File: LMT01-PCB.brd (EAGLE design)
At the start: 87 x 34.3 mm, 14 parts, among them IC3 PIC16F1826/27SO, IC4 MAX3467CPA, IC6 MCP23017SO

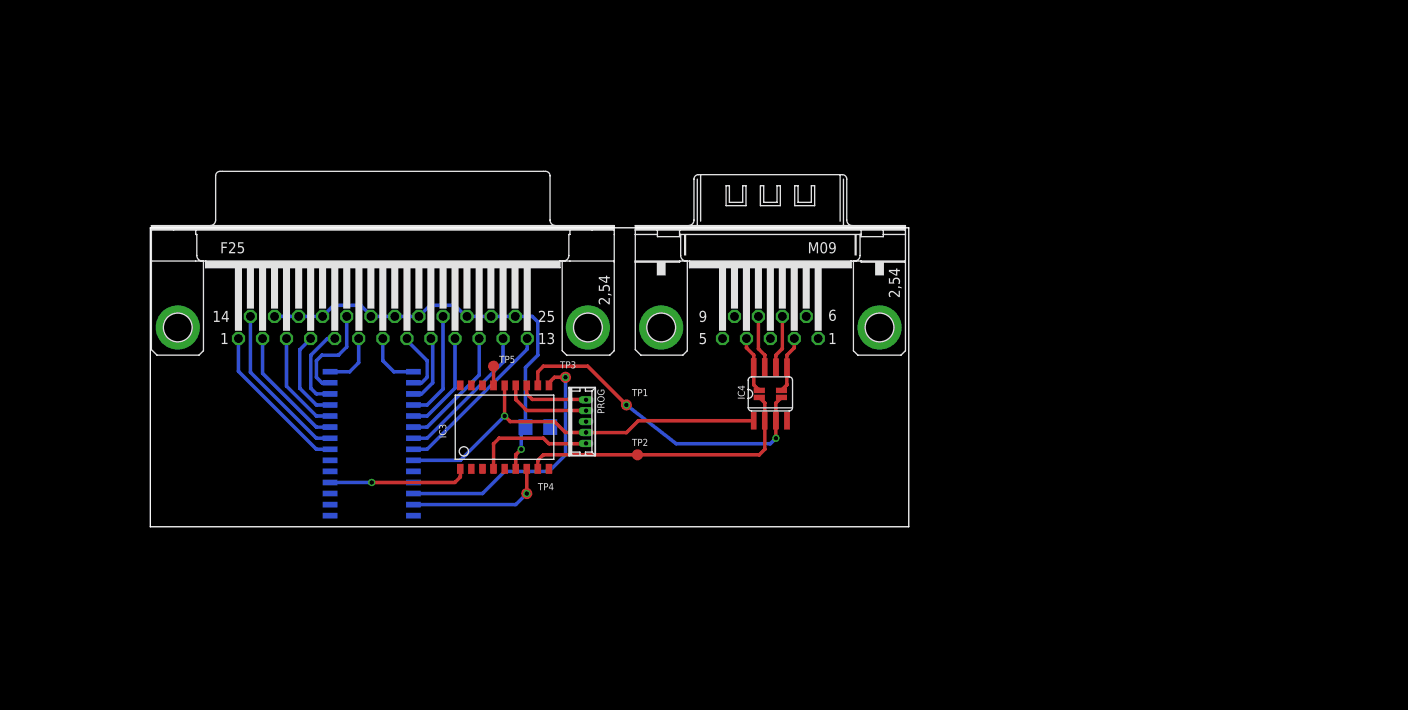
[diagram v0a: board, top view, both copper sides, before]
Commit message: Switching to big PIC
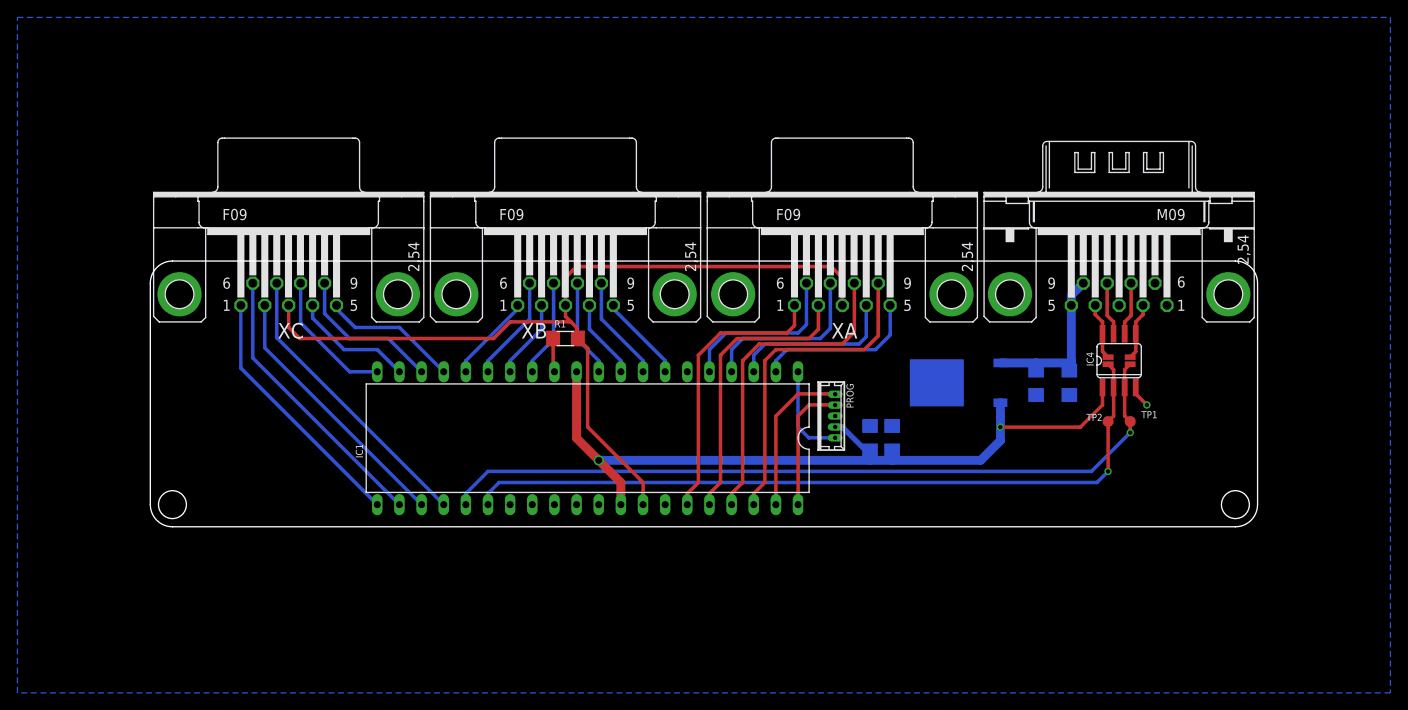
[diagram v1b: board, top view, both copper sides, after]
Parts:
- removed IC3: PIC16F1826/27SO, microchip:SO-18W
- removed IC6: MCP23017SO, microchip:SO28W
- removed TP3, TP4, TP5: TPB1,27, testpad:B1,27
- removed X1: (no value), con-subd:F25HP
- added C1, C2, C3, C4: (no value), resistor:C1206
- added IC1: PIC16F1517/19P, microchip:DIL40
- added U1: +12v, SparkFun-IC-Power:TO-252
- added XA, XB, XC: (no value), con-subd:F09HP
- moved TP1 57.8 mm to (112.4, 12.1)
- moved TP2 54.1 mm to (109.9, 12.1)
- moved JP1 40.2 mm to (109.9, 19.1)
- moved IC4 40.2 mm to (111.1, 19.1)
- moved JP2 40.2 mm to (112.4, 19.1)
- moved X2 40.2 mm to (111.1, 26.7)
- moved PROG 28.6 mm to (78.1, 12.7)
- moved R1 10.6 mm to (47.6, 21.6), flipped to the top
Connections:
- removed net !RST: IC3.1, IC6.18
- removed net N$10: IC6.26, X1.5
- removed net N$11: IC6.27, X1.18
- removed net N$12: IC6.28, X1.6
- removed net N$13: IC6.1, X1.7
- removed net N$14: IC6.2, X1.8
- removed net N$15: IC6.3, X1.9
- removed net N$16: IC6.4, X1.22
- removed net N$17: IC6.5, X1.10
- removed net N$18: IC6.6, X1.11
- removed net N$19: IC6.7, X1.12
- removed net N$20: IC6.8, X1.13
- removed net N$25: IC3.13, PROG.4
- removed net N$26: IC3.12, PROG.5
- removed net N$5: IC6.21, X1.1
- removed net N$6: IC6.22, X1.14
- removed net N$7: IC6.23, X1.2
- removed net N$8: IC6.24, X1.3
- removed net N$9: IC6.25, X1.4
- removed net SCL: IC3.10, IC6.12, TP3.TP
- removed net SDA: IC3.7, IC6.13, TP4.TP
- new net N$2: IC1.40, PROG.4
- new net TA1: IC1.35, XA.1
- new net TA2: IC1.5, XA.6
- new net TA3: IC1.36, XA.2
- new net TA4: IC1.4, XA.7
- new net TA5: IC1.37, XA.8
- new net TA6: IC1.3, XA.4
- new net TA7: IC1.38, XA.9
- new net TA8: IC1.2, XA.5
- new net TB1: IC1.16, XB.1
- new net TB2: IC1.15, XB.6
- new net TB3: IC1.14, XB.2
- new net TB4: IC1.13, XB.7
- new net TB5: IC1.10, XB.8
- new net TB6: IC1.9, XB.4
- new net TB7: IC1.8, XB.9
- new net TB8: IC1.7, XB.5
- new net TC1: IC1.21, XC.1
- new net TC2: IC1.22, XC.6
- new net TC3: IC1.23, XC.2
- new net TC4: IC1.24, XC.7
- new net TC5: IC1.20, XC.8
- new net TC6: IC1.19, XC.4
- new net TC7: IC1.18, XC.9
- new net TC8: IC1.17, XC.5
- net +5V: now also C3.1, C4.1, IC1.11, IC1.32, U1.2; no longer IC3.14, IC6.9
- net COMMON: now also IC1.33, XA.3, XB.3, XC.3; no longer IC3.6, X1.15, X1.16, X1.17, X1.19, X1.20, X1.21, X1.23, X1.24, X1.25
- net GND: now also C1.2, C2.2, C3.2, C4.2, IC1.12, IC1.31, U1.3; no longer IC3.5, IC6.10, IC6.15, IC6.16, IC6.17
- net N$1: now also IC1.1, PROG.1; no longer IC3.15, TP5.TP
- net N$3: now also IC1.39, PROG.5; no longer IC3.4, PROG.1
- net UARTRX: now also IC1.26; no longer IC3.8
- net UARTTX: now also IC1.25; no longer IC3.11
- net VCC: now also C1.1, C2.1, U1.1
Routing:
- net UARTRX: track 33.7 -> 86.3 mm, vias 0 -> 1
- net COMMON: track 50.5 -> 101.9 mm, vias 1 -> 0
- net UARTTX: track 37.7 -> 88.7 mm, vias 2 -> 1
- net +5V: track 46.0 -> 90.9 mm, vias 1 -> 2
- net TA7: track 0.00 -> 37.3 mm
- net TA5: track 0.00 -> 36.8 mm
- net TC4: track 0.00 -> 33.3 mm
- net TA3: track 0.00 -> 32.9 mm
- net TA1: track 0.00 -> 32.4 mm
- net TC2: track 0.00 -> 32.4 mm
- net SCL: track 30.6 -> 0.00 mm, vias 1 -> 0
- net TC3: track 0.00 -> 30.3 mm
- net TC1: track 0.00 -> 29.3 mm
- net TA4: track 0.00 -> 20.1 mm
- net VCC: track 0.00 -> 19.8 mm
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- added copper zone on layer 16, net GND
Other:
- board size 87 x 34.3 mm -> 127 x 30.5 mm

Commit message: PIC18
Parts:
- added C5, C6: (no value), resistor:C1206
- added R2, R3: (no value), resistor:R1206
- IC1: value PIC16F1517/19P -> PIC18F47K40
- moved R1 34.1 mm to (81.3, 15.9), turned to 90 degrees
- moved PROG 2.54 mm to (75.6, 12.7)
- moved IC1 2.54 mm to (47.6, 10.2)
- renumbered U1 to IC2
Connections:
- removed net COMMON: IC1.33, R1.2, XA.3, XB.3, XC.3
- new net COMMONA: IC1.36, R1.2, XA.3
- new net COMMONB: IC1.15, R2.2, XB.3
- new net COMMONC: IC1.25, R3.2, XC.3
- net +5V: now also C5.1, C6.1
- net GND: now also C5.2, C6.2, R2.1, R3.1
- net TA1: now also IC1.34; no longer IC1.35
- net TA3: now also IC1.35; no longer IC1.36
- net TB1: now also IC1.27; no longer IC1.16
- net TB2: now also IC1.14; no longer IC1.15
- net TB3: now also IC1.28; no longer IC1.14
- net TB5: now also IC1.29; no longer IC1.10
- net TB6: now also IC1.30; no longer IC1.9
- net TB7: now also IC1.10; no longer IC1.8
- net TB8: now also IC1.9; no longer IC1.7
- net UARTTX: now also IC1.33; no longer IC1.25
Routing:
- net COMMON: track 101.9 -> 0.00 mm
- net COMMONA: track 0.00 -> 63.4 mm
- net COMMONC: track 0.00 -> 30.7 mm
- net COMMONB: track 0.00 -> 27.4 mm
- net TB5: track 11.2 -> 29.0 mm
- net UARTTX: track 88.7 -> 71.0 mm
- net TB6: track 9.11 -> 25.6 mm
- net TB3: track 9.11 -> 25.4 mm
- net TB1: track 10.1 -> 25.3 mm
- net GND: track 6.41 -> 16.9 mm, vias 1 -> 2
- net +5V: track 90.9 -> 100.8 mm
- net TA3: track 32.9 -> 38.0 mm
- net TA1: track 32.4 -> 37.5 mm
- net TA7: track 37.3 -> 40.2 mm
- net TA5: track 36.8 -> 39.7 mm
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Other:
- board text added: "ELECTRONICS"
- board text added: "MEASUREMENT"
- board text added: "R1"
- board text added: "TEMPERATURE"

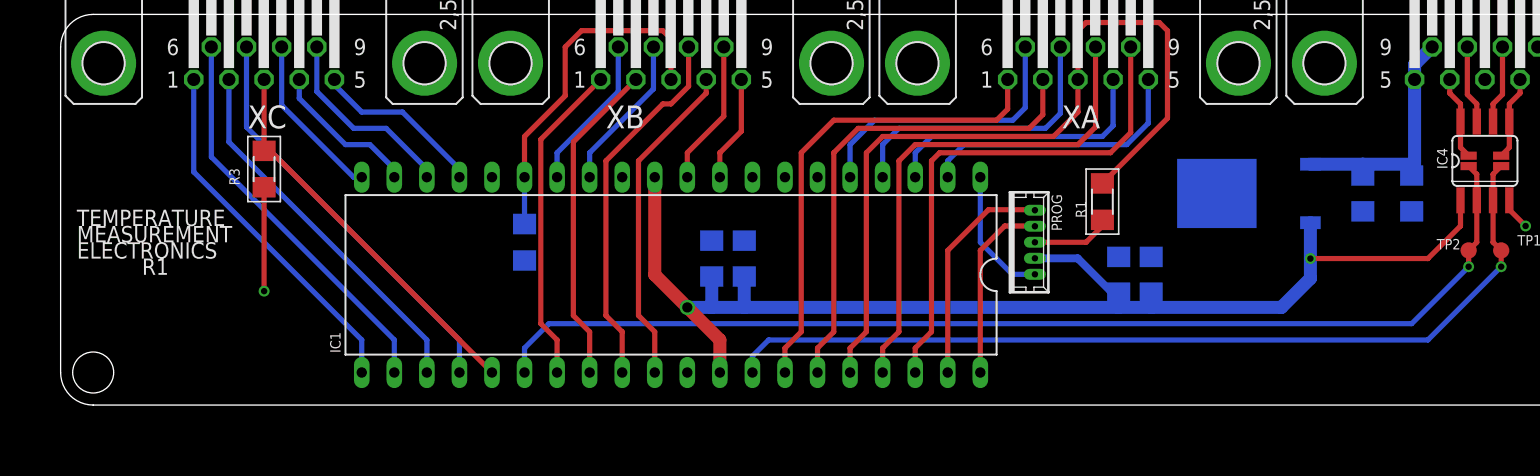
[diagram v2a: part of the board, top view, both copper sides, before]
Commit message: Adding optional comparators and voltage reference
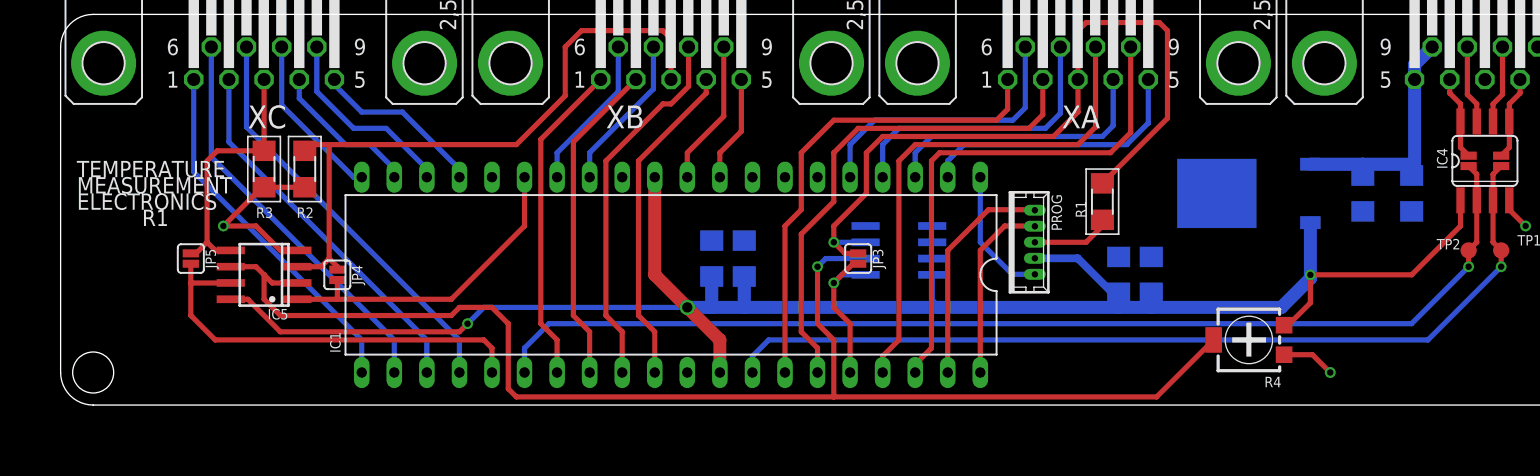
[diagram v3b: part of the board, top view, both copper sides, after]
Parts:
- added IC3, IC5: LM393D, linear:SO08
- added JP3, JP4, JP5: JUMPER-SMT_2_NO_SILK, SparkFun-Jumpers:SMT-JUMPER_2_NO_SILK
- added R4: (no value), resistor:RTRIM4G/J
- R1, R2, R3: value (none) -> 18.7k
- moved R2 18.1 mm to (19.1, 18.4), flipped to the top
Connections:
- new net COMMONA_BUF: IC1.36, IC3.1, JP3.2
- new net COMMONB_BUF: IC1.15, IC5.1, JP4.2
- new net COMMONC_BUF: IC1.25, IC5.7, JP5.2
- new net N$4: IC3.2, IC5.2, IC5.6, R4.2
- net +5V: now also IC3.8, IC5.8, R4.3
- net COMMONA: now also IC3.3, JP3.1; no longer IC1.36
- net COMMONB: now also IC5.3, JP4.1; no longer IC1.15
- net COMMONC: now also IC5.5, JP5.1; no longer IC1.25
- net GND: now also IC3.4, IC5.4, R4.1
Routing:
- net N$4: track 0.00 -> 104.9 mm, vias 0 -> 1
- net +5V: track 100.8 -> 146.5 mm, vias 2 -> 3
- net COMMONC_BUF: track 0.00 -> 33.6 mm
- net COMMONB_BUF: track 0.00 -> 25.4 mm
- net COMMONB: track 27.4 -> 50.9 mm
- net COMMONA_BUF: track 0.00 -> 12.8 mm, vias 0 -> 1
- net COMMONC: track 30.7 -> 20.4 mm
- net GND: track 16.9 -> 27.1 mm, vias 2 -> 3
- net COMMONA: track 63.4 -> 58.5 mm, vias 0 -> 1
- net TA3: track 38.0 -> 39.0 mm

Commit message: Adding power LED
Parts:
- added LED1: (no value), led:CHIPLED_1206
- added R5: (no value), resistor:R1206
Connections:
- new net N$5: LED1.A, R5.1
- net +5V: now also R5.2
- net GND: now also LED1.C
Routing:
- net GND: track 27.1 -> 36.1 mm
- net N$5: track 0.00 -> 3.18 mm
- net +5V: track 146.5 -> 149.2 mm
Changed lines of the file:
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@@
 <attribute name="NAME" x="11.303" y="11.43" size="0.8128" layer="25" font="fixed" ratio="20" rot="R270" align="bottom-center"/>
+</element>
+<element name="LED1" library="led" package="CHIPLED_1206" value="" x="109.22" y="7.62" smashed="yes" rot="R270">
+<attribute name="NAME" x="110.49" y="6.35" size="0.8128" layer="25" font="fixed" rot="R180"/>
+<attribute name="VALUE" x="107.95" y="5.08" size="1.27" layer="27"/>
+</element>
+<element name="R5" library="resistor" package="R1206" value="" x="102.87" y="7.62" smashed="yes" rot="R180">
+<attribute name="NAME" x="102.87" y="6.35" size="0.8128" layer="25" font="fixed" rot="R180"/>
+<attribute name="VALUE" x="104.14" y="10.16" size="1.27" layer="27" rot="R180"/>
 </element>
 </elements>
@@
 <wire x1="97.67" y1="3.93" x2="99.06" y2="2.54" width="0.4064" layer="1"/>
 <via x="99.06" y="2.54" extent="1-16" drill="0.5"/>
+<contactref element="LED1" pad="C"/>
+<wire x1="110.97" y1="7.62" x2="113.03" y2="7.62" width="0.4064" layer="1"/>
+<wire x1="113.03" y1="7.62" x2="114.3" y2="8.89" width="0.4064" layer="1"/>
+<wire x1="114.3" y1="8.89" x2="114.3" y2="13.97" width="0.4064" layer="1"/>
 </signal>
 <signal name="+5V">
@@
 <wire x1="109.22" y1="15.9766" x2="109.22" y2="13.97" width="0.4064" layer="1"/>
 <wire x1="109.22" y1="13.97" x2="105.41" y2="10.16" width="0.4064" layer="1"/>
-<wire x1="105.41" y1="10.16" x2="97.51" y2="10.16" width="0.4064" layer="1"/>
+<wire x1="105.41" y1="10.16" x2="101.6" y2="10.16" width="0.4064" layer="1"/>
 <via x="97.51" y="10.16" extent="1-16" drill="0.5"/>
 <contactref element="IC1" pad="32"/>
 <contactref element="IC1" pad="11"/>
+<wire x1="101.6" y1="10.16" x2="97.51" y2="10.16" width="0.4064" layer="1"/>
 <wire x1="46.355" y1="10.16" x2="46.355" y2="17.78" width="1.016" layer="1"/>
 <wire x1="51.435" y1="5.08" x2="51.435" y2="2.54" width="1.016" layer="1"/>
@@
 <wire x1="95.765" y1="6.23" x2="97.51" y2="7.975" width="0.4064" layer="1"/>
 <wire x1="97.51" y1="10.16" x2="97.51" y2="7.975" width="0.4064" layer="1"/>
+<contactref element="R5" pad="2"/>
+<wire x1="101.448" y1="7.62" x2="101.6" y2="7.62" width="0.4064" layer="1"/>
+<wire x1="101.6" y1="7.62" x2="101.6" y2="10.16" width="0.4064" layer="1"/>
 </signal>
 <signal name="UARTRX">
@@
 <wire x1="10.16" y1="9.525" x2="10.16" y2="11.0236" width="0.4064" layer="1"/>
 </signal>
+<signal name="N$5">
+<contactref element="LED1" pad="A"/>
+<contactref element="R5" pad="1"/>
+<wire x1="104.292" y1="7.62" x2="107.47" y2="7.62" width="0.4064" layer="1"/>
+</signal>
 </signals>

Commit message: Upgrading to PIC18F47Q84
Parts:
- IC1: value PIC18F47K40 -> PIC18F47Q84; device microchip:DIL40 -> FRC696:DIL40
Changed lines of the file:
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@@
 <attribute name="VALUE" x="82.55" y="8.89" size="1.27" layer="28" rot="MR90"/>
 </element>
-<element name="IC1" library="microchip" package="DIL40" value="PIC18F47K40" x="47.625" y="10.16" smashed="yes" rot="R180">
+<element name="IC1" library="FRC696" package="DIL40" value="PIC18F47Q84" x="47.625" y="10.16" smashed="yes" rot="R180">
 <attribute name="NAME" x="21.844" y="4.064" size="0.8128" layer="25" font="fixed" ratio="10" rot="R90"/>
 </element>
